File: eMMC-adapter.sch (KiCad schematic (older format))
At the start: 9 parts, among them J1 Micro_SD_Card, U1 eMMC_5.1_BGA153

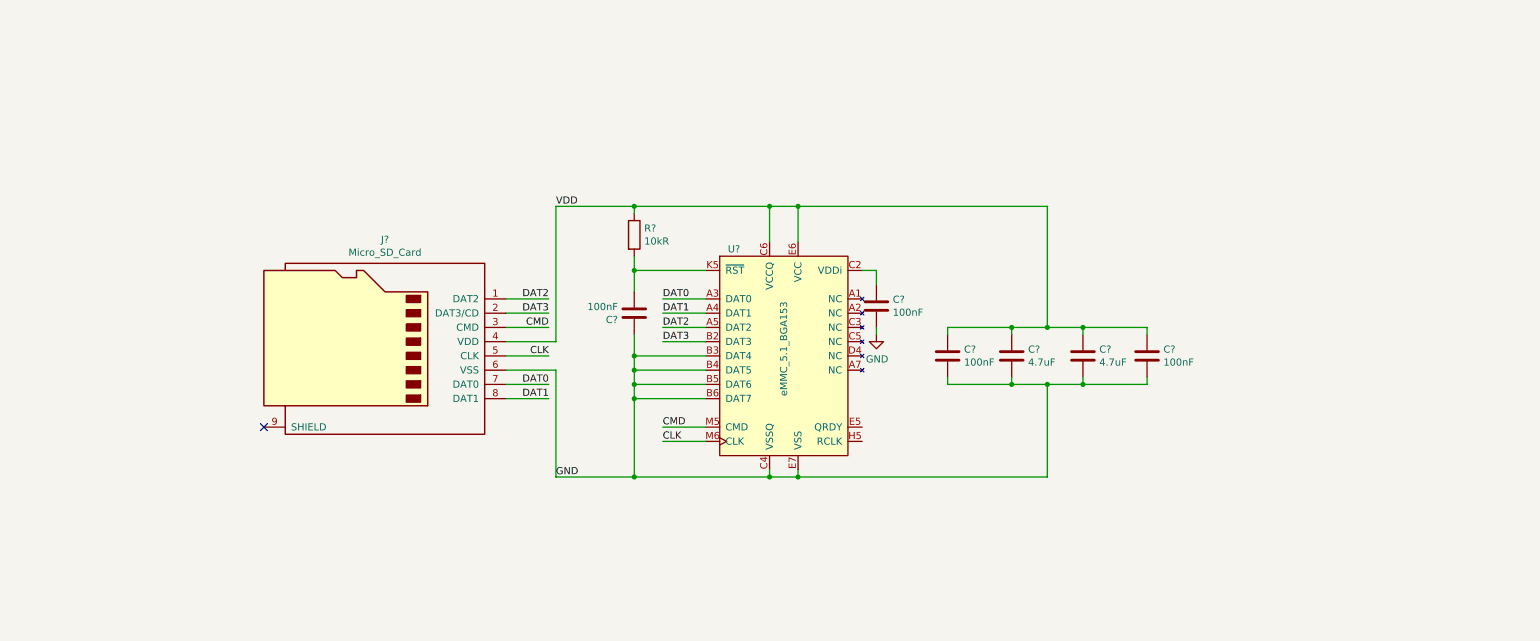
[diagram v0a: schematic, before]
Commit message: Redo termination and layout of first module
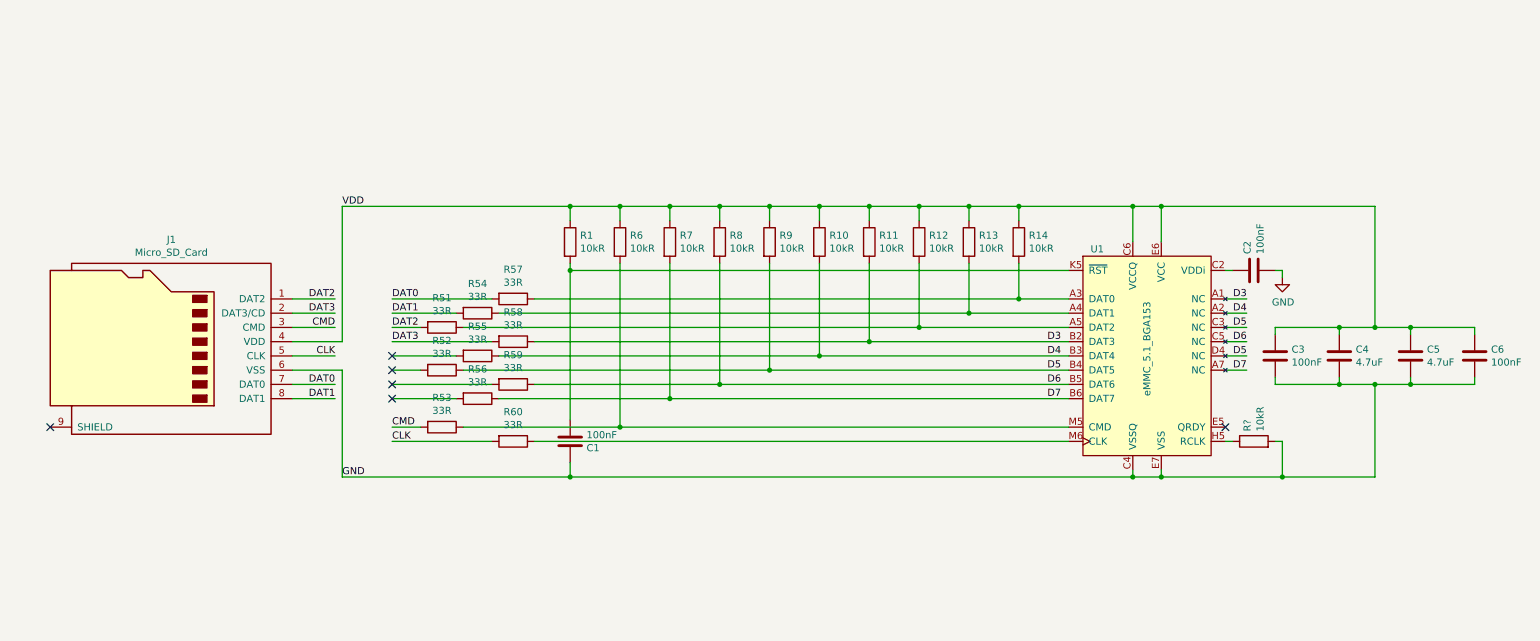
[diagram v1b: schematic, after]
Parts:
- added R42, R43, R44, R45, R46, R47, R48, R49, R50, R?: 10kR, Resistor_SMD:R_0402_1005Metric, symbol Device:R
- added R51, R52, R53, R54, R55, R56, R57, R58, R59, R60: 33R, Resistor_SMD:R_0402_1005Metric, symbol Device:R
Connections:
- net CLK: now also R60.2; no longer U1.M6 (CLK)
- net CMD: now also R53.2; no longer U1.M5 (CMD)
- net DAT0: now also R57.2; no longer U1.A3 (DAT0)
- net DAT1: now also R54.2; no longer U1.A4 (DAT1)
- net DAT2: now also R51.2; no longer U1.A5 (DAT2)
- net DAT3: now also R58.2; no longer U1.B2 (DAT3)
- net GND: now also R?.2; no longer U1.B3 (DAT4), U1.B4 (DAT5), U1.B5 (DAT6), U1.B6 (DAT7)
- net VCC: now also R42.1, R43.1, R44.1, R45.1, R46.1, R47.1, R48.1, R49.1, R50.1
- net D3: now reaches U1.A1 (NC)
- net D3: now also U1.B2 (DAT3), R47.2, R58.1
- net D4: now reaches U1.A2 (NC)
- net D4: now also U1.B3 (DAT4), R46.2, R55.1
- net D7: now reaches U1.A7 (NC)
- net D7: now also U1.B6 (DAT7), R43.2, R56.1
- net D5: now reaches U1.C3 (NC)
- net D5: now also U1.B4 (DAT5), U1.D4 (NC), R45.2, R52.1
- net D6: now reaches U1.C5 (NC)
- net D6: now also U1.B5 (DAT6), R44.2, R59.1
- net at U1.H5 (RCLK): now also R?.1
- new net: R50.2, R57.1, U1.A3 (DAT0)
- new net: R49.2, R54.1, U1.A4 (DAT1)
- new net: R48.2, R51.1, U1.A5 (DAT2)
- new net: R42.2, R53.1, U1.M5 (CMD)
- new net: R60.1, U1.M6 (CLK)
- no-connect marks 1 -> 6
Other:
- moved on the sheet: C1, C2, C3, C4, C5, C6, J1, R1, U1

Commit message: Add mousebites to first adapter
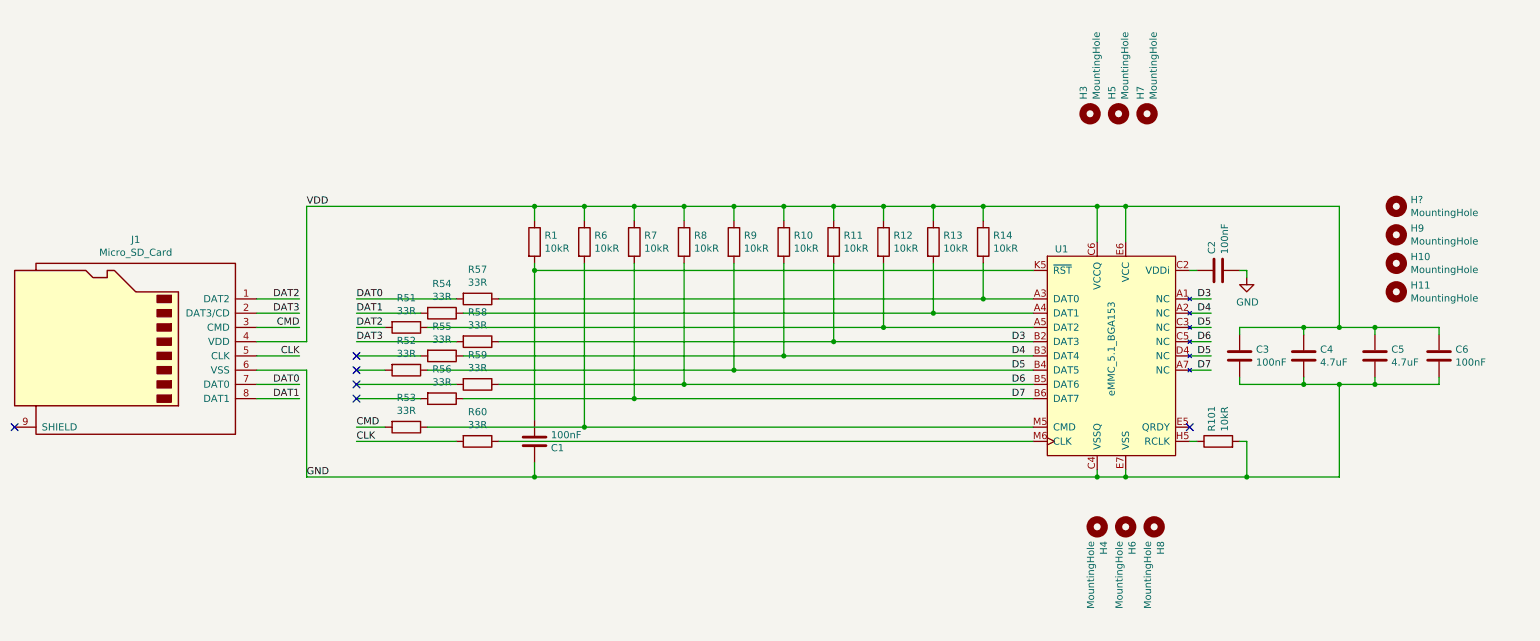
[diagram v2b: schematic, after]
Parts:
- added H10, H11, H3, H4, H5, H6, H7, H8, H9, H?: MountingHole, Perforation:Perforation_0.3mm, symbol Mechanical:MountingHole
- gave numbers to parts that had none: 1
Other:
- moved on the sheet: C1, C2, C3, C4, C5, C6, J1, R1, R10, R101, R11, R12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

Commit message: Fix missing LCSC partnumbers
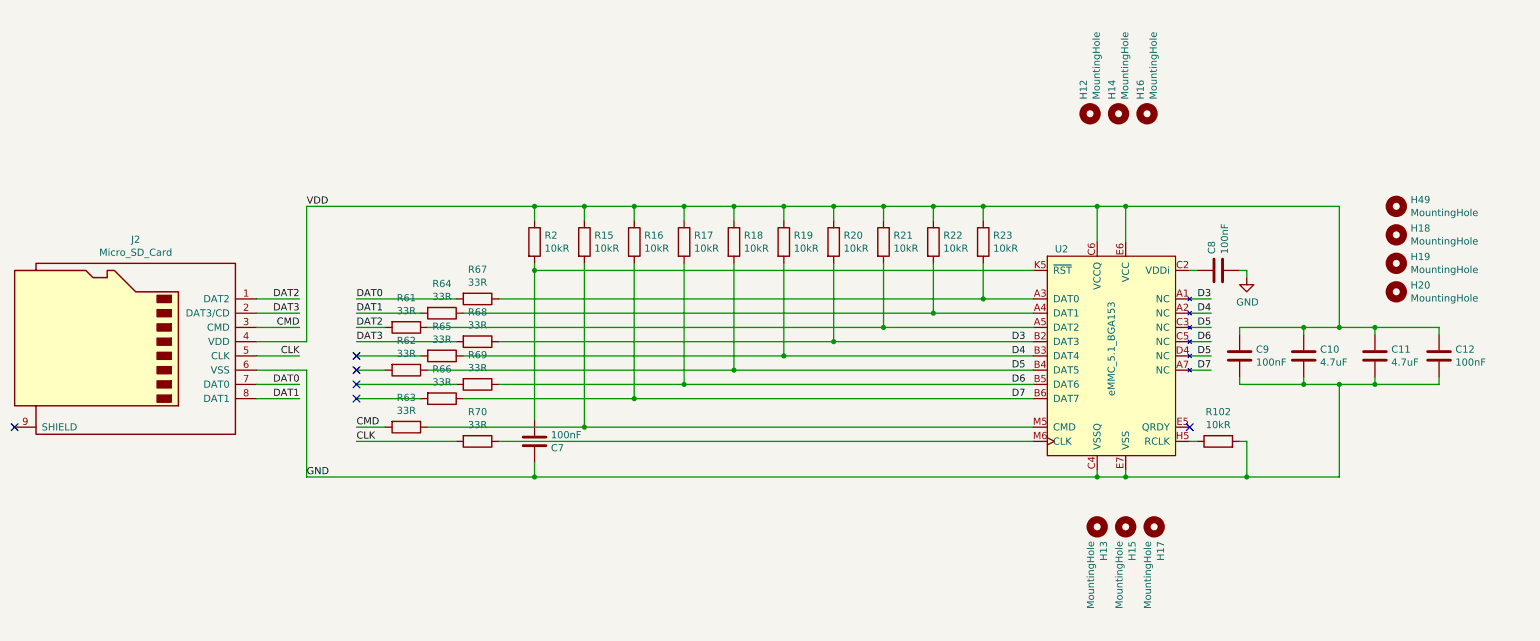
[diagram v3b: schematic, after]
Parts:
- R1, R101: LCSC (none) -> C25744
- gave numbers to parts that had none: 1
